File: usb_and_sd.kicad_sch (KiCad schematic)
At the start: 72 parts, among them J6001 USB_C_Receptacle_USB2.0_16P, J6002 USB_A, J6003 Micro_SD_Card_Det1, U1002 AM6231ASGGGAALW, U6001 TVS0500DRVR, U6002 SDINBDG4-16G, U6003 TPD3S014, U6004 TPS22918DBVR

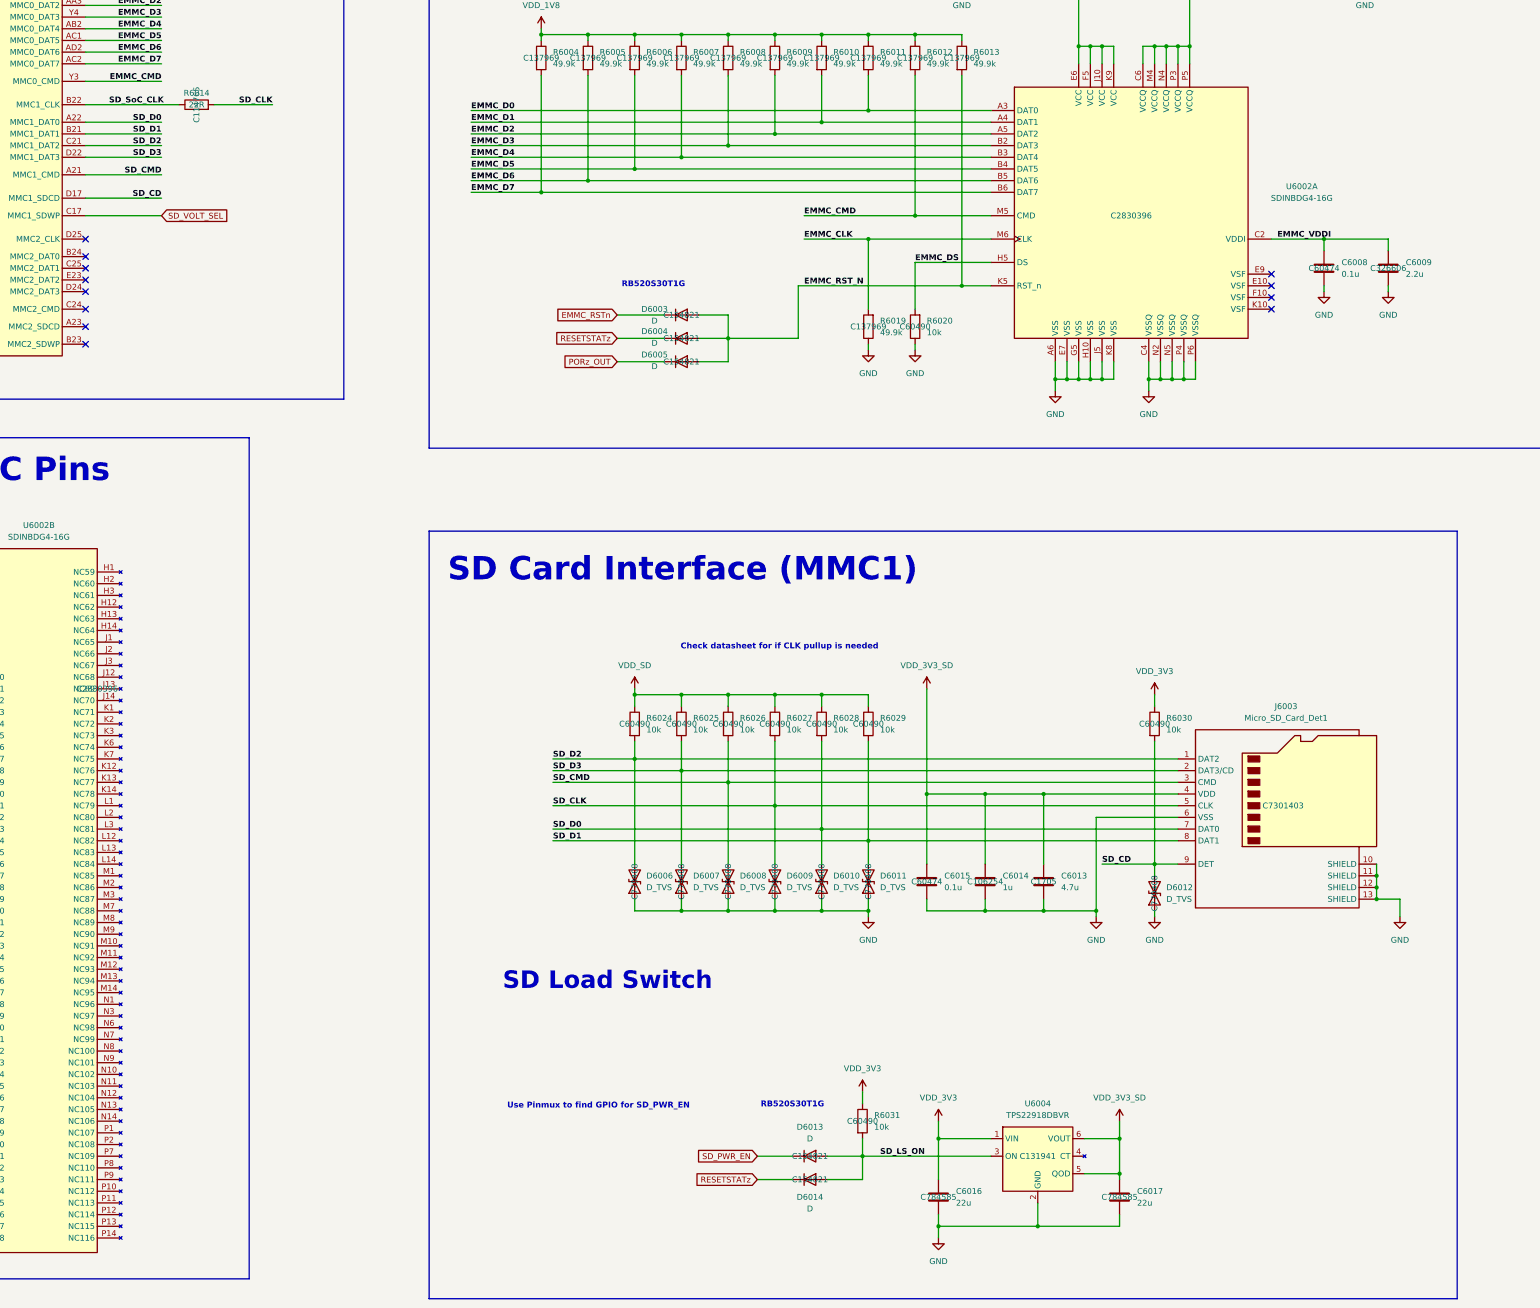
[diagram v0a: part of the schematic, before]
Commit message: Fixed MGM240P pinout, replaced 01x06 SPI and UART header pins with 02x06 header pins that will be connected via jumper shunts, deleted MMC1 (microSD)
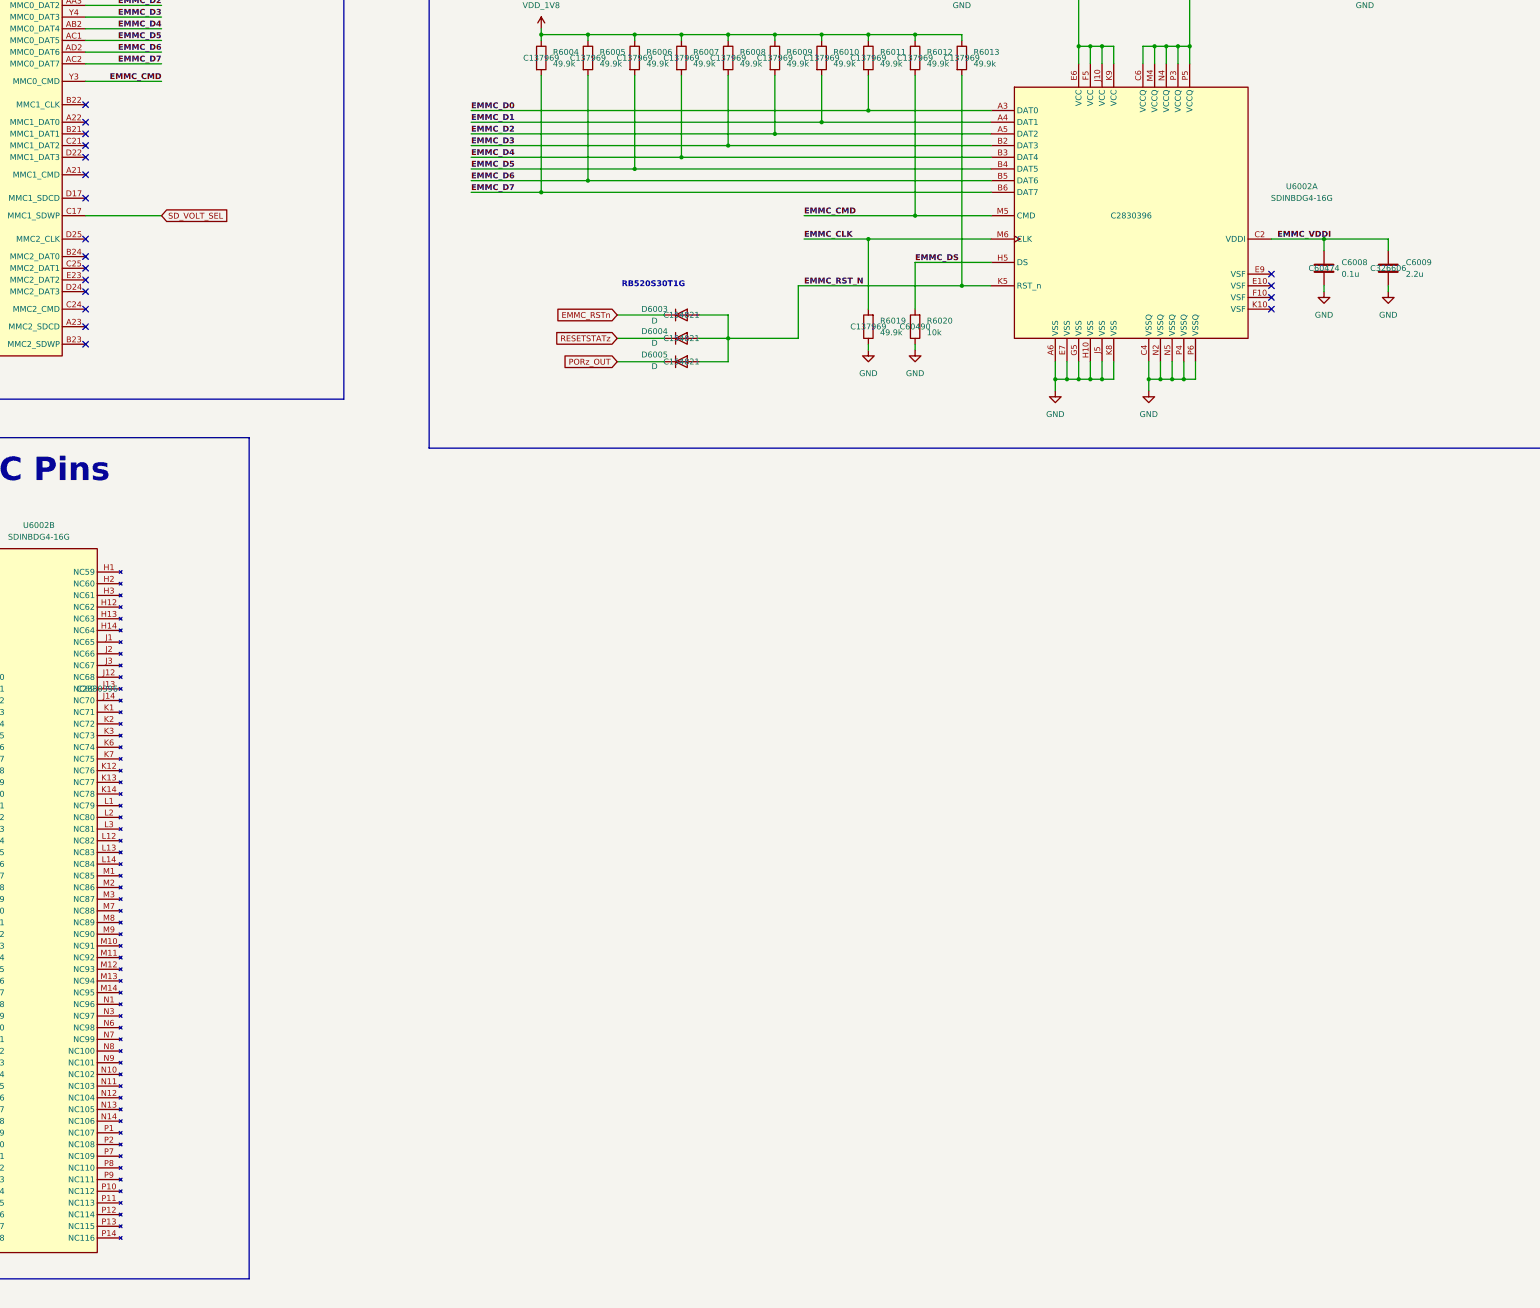
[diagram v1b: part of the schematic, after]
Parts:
- removed C6013: 4.7u, Capacitor_SMD:C_0603_1608Metric, symbol Device:C
- removed C6014: 1u, Capacitor_SMD:C_0402_1005Metric, symbol Device:C
- removed C6015: 0.1u, Capacitor_SMD:C_0402_1005Metric, symbol Device:C
- removed C6016, C6017: 22u, Capacitor_SMD:C_0805_2012Metric, symbol Device:C
- removed D6006, D6007, D6008, D6009, D6010, D6011, D6012: D_TVS, SoftServicesFootprintLibrary:TPD1E1B04DPYR, symbol Device:D_TVS
- removed D6013, D6014: D, Diode_SMD:D_SOD-523, symbol Device:D
- removed J6003: Micro_SD_Card_Det1, MEM2052-00-195-00-A:MEM20520019500A, symbol Connector:Micro_SD_Card_Det1
- removed R6014: 22R, Resistor_SMD:R_0402_1005Metric, symbol Device:R
- removed R6024, R6025, R6026, R6027, R6028, R6029, R6030, R6031: 10k, Resistor_SMD:R_0402_1005Metric, symbol Device:R
- removed U6004: TPS22918DBVR, TPS22918DBVR:SOT95P280X145-6N, symbol SoftServicesSymbolLibrary:TPS22918DBVR
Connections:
- net SD_CD: no longer names the net of U1002.D17 (MMC1_SDCD)
- net SD_CMD: no longer names the net of U1002.A21 (MMC1_CMD)
- net SD_D0: no longer names the net of U1002.A22 (MMC1_DAT0)
- net SD_D1: no longer names the net of U1002.B21 (MMC1_DAT1)
- net SD_D2: no longer names the net of U1002.C21 (MMC1_DAT2)
- net SD_D3: no longer names the net of U1002.D22 (MMC1_DAT3)
- net SD_SoC_CLK: no longer names the net of U1002.B22 (MMC1_CLK)
- no-connect marks 15 -> 22
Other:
- note removed: "Check datasheet for if CLK pullup is needed"
- note removed: "SD Card Interface (MMC1)"
- note removed: "SD Load Switch"
- note removed: "Use Pinmux to find GPIO for SD_PWR_EN"
